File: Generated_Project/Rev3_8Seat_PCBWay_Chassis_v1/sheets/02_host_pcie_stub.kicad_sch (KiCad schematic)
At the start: 0 parts

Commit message: Raise Rev3 chassis to 8 electrically designed seats.
Name v1.0 power/PE/clock nets on all eight OAM seats toward two DNP
PM8536B-FEI (x8 per GCD), keep SB175 star + local P48V pours, and generate
the 12-layer 2.0 mm stuffed-switch target. First stuffing may still populate
two modules; the PCB does not need a respin for the other six.

Do not fabricate. Do not energize P48V.

Co-authored-by: zivzancoeli-commits <zivzancoeli-commits@users.noreply.github.com>
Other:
- note added: "PURPOSE: Named v1.0 PCIE_TXnP/N and PCIE_RXnP/N (n=0..15) on ALL 8 seats. 8 electrically designed seats. First stuffing may populate 2 modules / 6 DNP — the PCB does not require a respin for the other six. OCP pin list (module POV): - PETp/n = module TX, host RX. AC caps on motherboard/carrier — not placed. - PERp/n = module RX, host TX. AC caps on motherboard/carrier — not placed. This sheet doe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"
- note removed: "PURPOSE: Host PCIe stub using ONLY v1.0 names PCIE_TXnP/N and PCIE_RXnP/N (n=0..15). THIS SHEET IS SEATS 0 AND 1 ONLY. OCP pin list (module POV): - PETp/n = module TX, host RX. AC caps on motherboard/carrier — not placed. - PERp/n = module RX, host TX. AC caps on motherboard/carrier — not placed. This sheet does NOT map those pairs onto a CEM x16 connector pinout. Do NOT invent a CEM cable, SlimS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"
- title: Host PCIe stub (OAM0-OAM1 only) -> Host PE stub (all 8 seats via DNP PM8536)

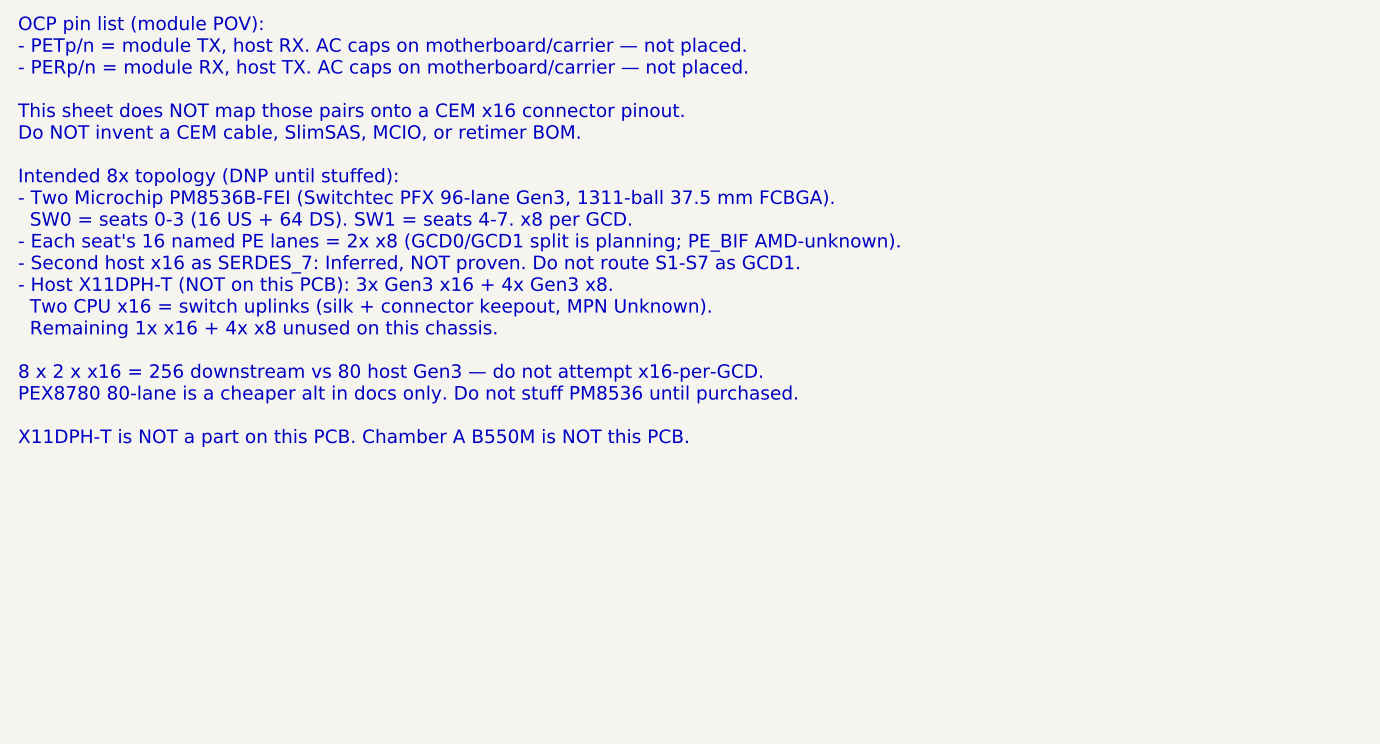
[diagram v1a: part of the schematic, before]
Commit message: Label PEX8780-AB80BI G as the only switch CANDIDATE (DNP).
Keepout is one 35 mm 1156-FCBGA for 8x x8 Gen3 plus one x16 host uplink.
Do not invent a second MPN. Do not stuff. 8-layer is likely if this BGA
is ever assembled; PCBWay 1156-FCBGA attach remains Unknown.

Still do not fabricate or energize P48V. No xGMI, no CEM.

Co-authored-by: zivzancoeli-commits <zivzancoeli-commits@users.noreply.github.com>
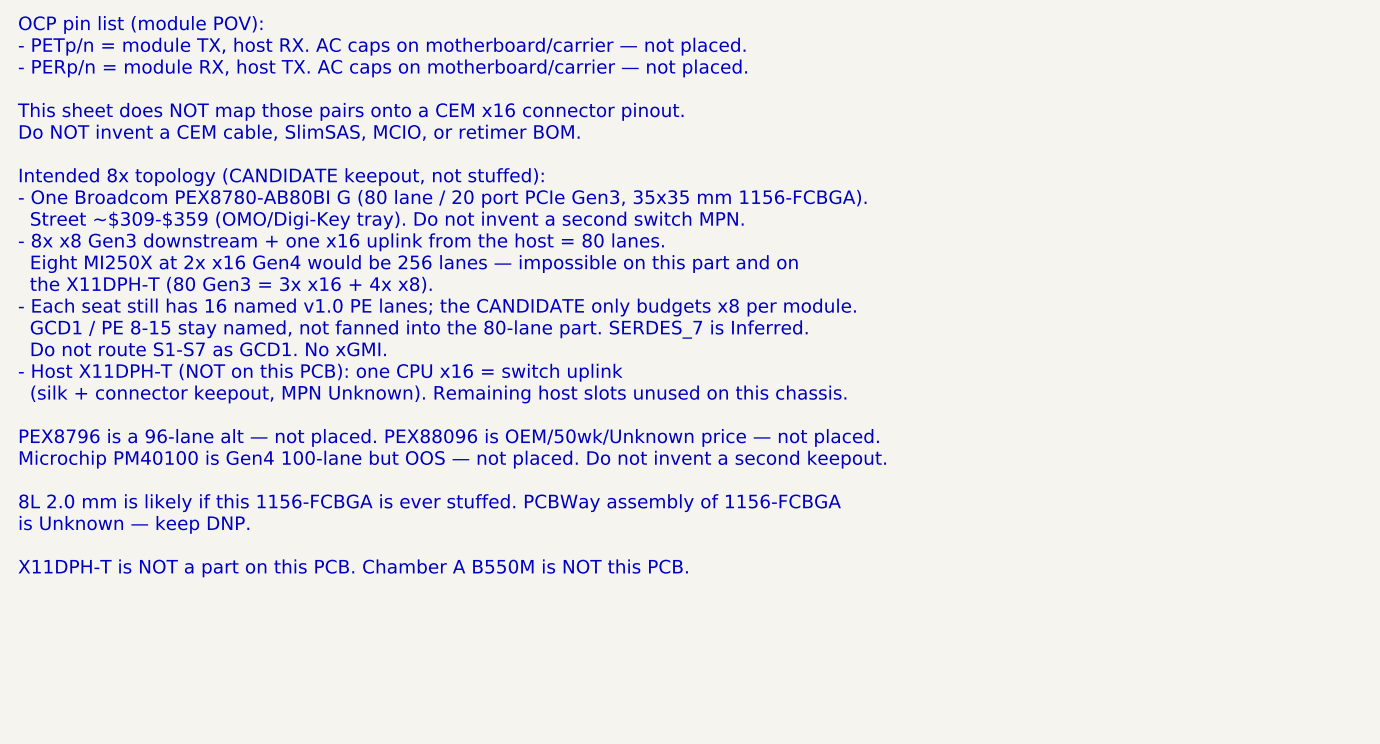
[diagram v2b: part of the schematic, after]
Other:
- title: Host PE stub (all 8 seats via DNP PM8536) -> Host PE stub (all 8 seats via PEX8780 CANDIDATE)
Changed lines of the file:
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@@
 	(paper "A3")
 	(title_block
-		(title "Host PE stub (all 8 seats via DNP PM8536)")
+		(title "Host PE stub (all 8 seats via PEX8780 CANDIDATE)")
 		(date "2026-08-21")
 		(rev "Rev3_8Seat_PCBWay_v1")
@@
         (comment 4 "r2.0 UNUSABLE. P3V3=Conn0 C1/C2. 12L 2.0mm stuffed-switch TARGET. Star-fed P48V.")
 	)
-	(text "PURPOSE: Named v1.0 PCIE_TXnP/N and PCIE_RXnP/N (n=0..15) on ALL 8 seats.\n\n8 electrically designed seats. First stuffing may populate 2 modules / 6 DNP —\nthe PCB does not require a respin for the other six.\n\nOCP pin list (module POV):\n- PETp/n = module TX, host RX. AC caps on motherboard/carrier — not placed.\n- PERp/n = module RX, host TX. AC caps on motherboard/carrier — not placed.\n\nThis sheet does NOT map those pairs onto a CEM x16 connector pinout.\nDo NOT invent a CEM cable, SlimSAS, MCIO, or retimer BOM.\n\nIntended 8x topology (DNP until stuffed):\n- Two Microchip PM8536B-FEI (Switchtec PFX 96-lane Gen3, 1311-ball 37.5 mm FCBGA).\n  SW0 = seats 0-3 (16 US + 64 DS). SW1 = seats 4-7. x8 per GCD.\n- Each seat's 16 named PE lanes = 2x x8 (GCD0/GCD1 split is planning; PE_BIF AMD-unknown).\n- Second host x16 as SERDES_7: Inferred, NOT proven. Do not route S1-S7 as GCD1.\n- Host X11DPH-T (NOT on this PCB): 3x Gen3 x16 + 4x Gen3 x8.\n  Two CPU x16 = switch uplinks (silk + connector keepout, MPN Unknown).\n  Remaining 1x x16 + 4x x8 unused on this chassis.\n\n8 x 2 x x16 = 256 downstream vs 80 host Gen3 — do not attempt x16-per-GCD.\nPEX8780 80-lane is a cheaper alt in docs only. Do not stuff PM8536 until purchased.\n\nX11DPH-T is NOT a part on this PCB. Chamber A B550M is NOT this PCB.\n"
+	(text "PURPOSE: Named v1.0 PCIE_TXnP/N and PCIE_RXnP/N (n=0..15) on ALL 8 seats.\n\n8 electrically designed seats. First stuffing may populate 2 modules / 6 DNP —\nthe PCB does not require a respin for the other six.\n\nOCP pin list (module POV):\n- PETp/n = module TX, host RX. AC caps on motherboard/carrier — not placed.\n- PERp/n = module RX, host TX. AC caps on motherboard/carrier — not placed.\n\nThis sheet does NOT map those pairs onto a CEM x16 connector pinout.\nDo NOT invent a CEM cable, SlimSAS, MCIO, or retimer BOM.\n\nIntended 8x topology (CANDIDATE keepout, not stuffed):\n- One Broadcom PEX8780-AB80BI G (80 lane / 20 port PCIe Gen3, 35x35 mm 1156-FCBGA).\n  Street ~$309-$359 (OMO/Digi-Key tray). Do not invent a second switch MPN.\n- 8x x8 Gen3 downstream + one x16 uplink from the host = 80 lanes.\n  Eight MI250X at 2x x16 Gen4 would be 256 lanes — impossible on this part and on\n  the X11DPH-T (80 Gen3 = 3x x16 + 4x x8).\n- Each seat still has 16 named v1.0 PE lanes; the CANDIDATE only budgets x8 per module.\n  GCD1 / PE 8-15 stay named, not fanned into the 80-lane part. SERDES_7 is Inferred.\n  Do not route S1-S7 as GCD1. No xGMI.\n- Host X11DPH-T (NOT on this PCB): one CPU x16 = switch uplink\n  (silk + connector keepout, MPN Unknown). Remaining host slots unused on this chassis.\n\nPEX8796 is a 96-lane alt — not placed. PEX88096 is OEM/50wk/Unknown price — not placed.\nMicrochip PM40100 is Gen4 100-lane but OOS — not placed. Do not invent a second keepout.\n\n8L 2.0 mm is likely if this 1156-FCBGA is ever stuffed. PCBWay assembly of 1156-FCBGA\nis Unknown — keep DNP.\n\nX11DPH-T is NOT a part on this PCB. Chamber A B550M is NOT this PCB.\n"
 		(exclude_from_sim no)
 		(at 20.32 20.32 0)

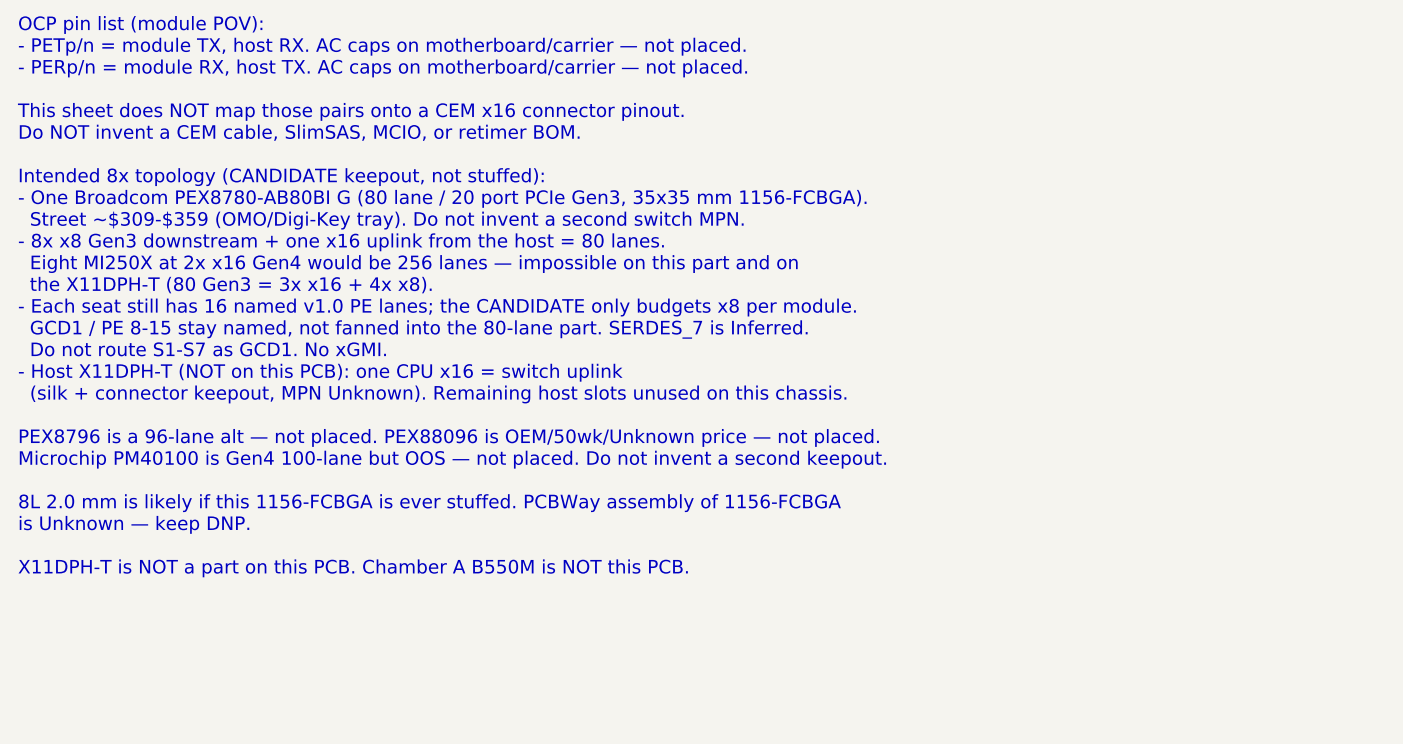
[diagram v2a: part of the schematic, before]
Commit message: Make PM8536B-FEI the PRIMARY switch keepout (DNP x2).
Two 37.5 mm 1311-FCBGA courtyards, x8 per GCD (SW0 seats 0-3, SW1 4-7),
two CPU x16 uplinks. PEX8780 stays a cheaper 80-lane alt in docs only.
GCD1 = SERDES_7 remains Inferred. No CEM, no xGMI, do not fabricate.

Co-authored-by: zivzancoeli-commits <zivzancoeli-commits@users.noreply.github.com>
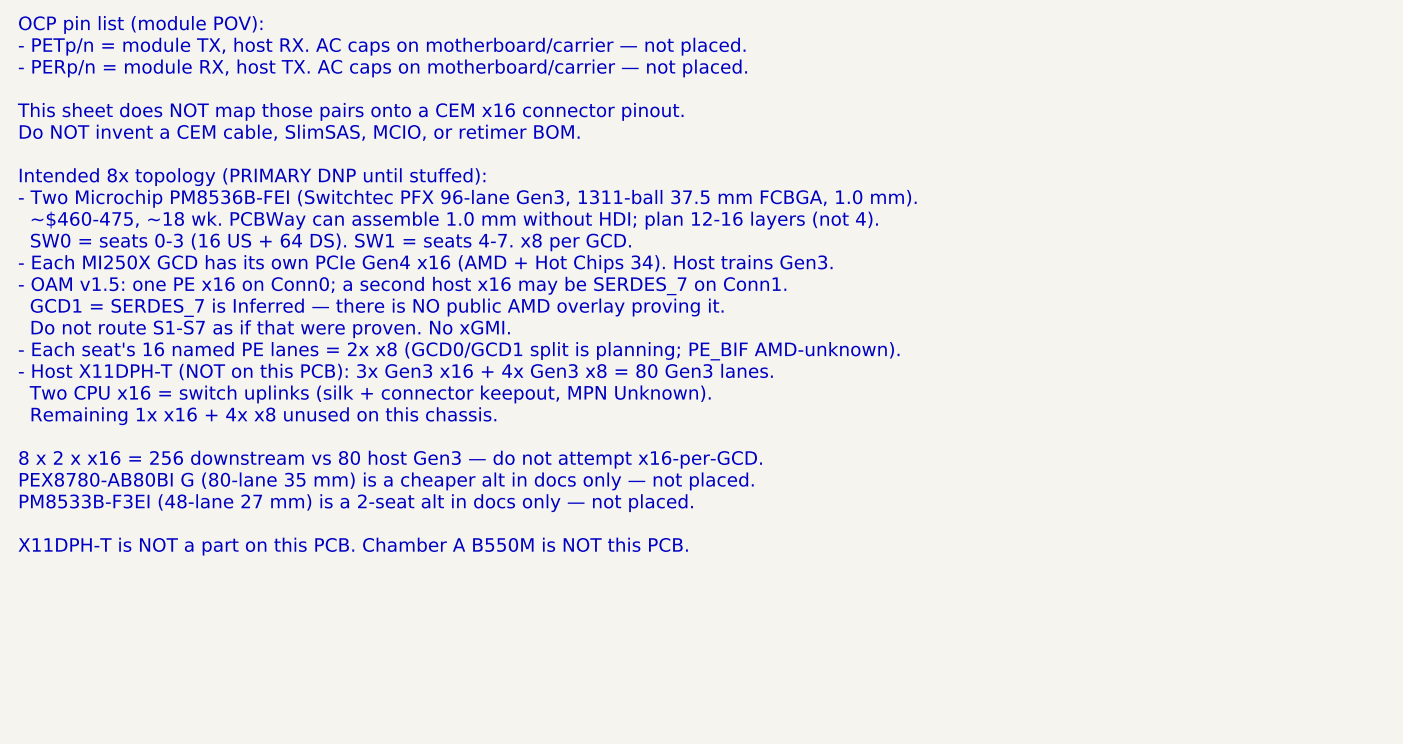
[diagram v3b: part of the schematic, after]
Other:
- title: Host PE stub (all 8 seats via PEX8780 CANDIDATE) -> Host PE stub (all 8 seats via DNP PM8536 PRIMARY)
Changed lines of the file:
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@@
 	(paper "A3")
 	(title_block
-		(title "Host PE stub (all 8 seats via PEX8780 CANDIDATE)")
+		(title "Host PE stub (all 8 seats via DNP PM8536 PRIMARY)")
 		(date "2026-08-21")
 		(rev "Rev3_8Seat_PCBWay_v1")
@@
         (comment 2 "Documentation sheet — no invented nets")
         (comment 3 "Pin names: OAM Pin map rev 1.0.xlsx — OCP generic, NOT AMD overlay")
-        (comment 4 "r2.0 UNUSABLE. P3V3=Conn0 C1/C2. 12L 2.0mm stuffed-switch TARGET. Star-fed P48V.")
+        (comment 4 "r2.0 UNUSABLE. P3V3=Conn0 C1/C2. 12L 2.0mm stuffed-switch TARGET. 2x PM8536 DNP. Star-fed P48V.")
 	)
-	(text "PURPOSE: Named v1.0 PCIE_TXnP/N and PCIE_RXnP/N (n=0..15) on ALL 8 seats.\n\n8 electrically designed seats. First stuffing may populate 2 modules / 6 DNP —\nthe PCB does not require a respin for the other six.\n\nOCP pin list (module POV):\n- PETp/n = module TX, host RX. AC caps on motherboard/carrier — not placed.\n- PERp/n = module RX, host TX. AC caps on motherboard/carrier — not placed.\n\nThis sheet does NOT map those pairs onto a CEM x16 connector pinout.\nDo NOT invent a CEM cable, SlimSAS, MCIO, or retimer BOM.\n\nIntended 8x topology (CANDIDATE keepout, not stuffed):\n- One Broadcom PEX8780-AB80BI G (80 lane / 20 port PCIe Gen3, 35x35 mm 1156-FCBGA).\n  Street ~$309-$359 (OMO/Digi-Key tray). Do not invent a second switch MPN.\n- 8x x8 Gen3 downstream + one x16 uplink from the host = 80 lanes.\n  Eight MI250X at 2x x16 Gen4 would be 256 lanes — impossible on this part and on\n  the X11DPH-T (80 Gen3 = 3x x16 + 4x x8).\n- Each seat still has 16 named v1.0 PE lanes; the CANDIDATE only budgets x8 per module.\n  GCD1 / PE 8-15 stay named, not fanned into the 80-lane part. SERDES_7 is Inferred.\n  Do not route S1-S7 as GCD1. No xGMI.\n- Host X11DPH-T (NOT on this PCB): one CPU x16 = switch uplink\n  (silk + connector keepout, MPN Unknown). Remaining host slots unused on this chassis.\n\nPEX8796 is a 96-lane alt — not placed. PEX88096 is OEM/50wk/Unknown price — not placed.\nMicrochip PM40100 is Gen4 100-lane but OOS — not placed. Do not invent a second keepout.\n\n8L 2.0 mm is likely if this 1156-FCBGA is ever stuffed. PCBWay assembly of 1156-FCBGA\nis Unknown — keep DNP.\n\nX11DPH-T is NOT a part on this PCB. Chamber A B550M is NOT this PCB.\n"
+	(text "PURPOSE: Named v1.0 PCIE_TXnP/N and PCIE_RXnP/N (n=0..15) on ALL 8 seats.\n\n8 electrically designed seats. First stuffing may populate 2 modules / 6 DNP —\nthe PCB does not require a respin for the other six.\n\nOCP pin list (module POV):\n- PETp/n = module TX, host RX. AC caps on motherboard/carrier — not placed.\n- PERp/n = module RX, host TX. AC caps on motherboard/carrier — not placed.\n\nThis sheet does NOT map those pairs onto a CEM x16 connector pinout.\nDo NOT invent a CEM cable, SlimSAS, MCIO, or retimer BOM.\n\nIntended 8x topology (PRIMARY DNP until stuffed):\n- Two Microchip PM8536B-FEI (Switchtec PFX 96-lane Gen3, 1311-ball 37.5 mm FCBGA, 1.0 mm).\n  ~$460-475, ~18 wk. PCBWay can assemble 1.0 mm without HDI; plan 12-16 layers (not 4).\n  SW0 = seats 0-3 (16 US + 64 DS). SW1 = seats 4-7. x8 per GCD.\n- Each MI250X GCD has its own PCIe Gen4 x16 (AMD + Hot Chips 34). Host trains Gen3.\n- OAM v1.5: one PE x16 on Conn0; a second host x16 may be SERDES_7 on Conn1.\n  GCD1 = SERDES_7 is Inferred — there is NO public AMD overlay proving it.\n  Do not route S1-S7 as if that were proven. No xGMI.\n- Each seat's 16 named PE lanes = 2x x8 (GCD0/GCD1 split is planning; PE_BIF AMD-unknown).\n- Host X11DPH-T (NOT on this PCB): 3x Gen3 x16 + 4x Gen3 x8 = 80 Gen3 lanes.\n  Two CPU x16 = switch uplinks (silk + connector keepout, MPN Unknown).\n  Remaining 1x x16 + 4x x8 unused on this chassis.\n\n8 x 2 x x16 = 256 downstream vs 80 host Gen3 — do not attempt x16-per-GCD.\nPEX8780-AB80BI G (80-lane 35 mm) is a cheaper alt in docs only — not placed.\nPM8533B-F3EI (48-lane 27 mm) is a 2-seat alt in docs only — not placed.\n\nX11DPH-T is NOT a part on this PCB. Chamber A B550M is NOT this PCB.\n"
 		(exclude_from_sim no)
 		(at 20.32 20.32 0)
